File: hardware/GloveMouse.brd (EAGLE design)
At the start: 45.4 x 54.5 mm, 46 parts, among them IC3 MCP73811/2, J1 USB MICRO, U1 ATMEGA32U4-XUAU, U4 MCP1825S-3302E/DB

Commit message: GloveMouse v2.1 all-in-one commit
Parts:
- removed PARANI: (no value), pinhead:2X06
- added R1: 220, resistor:R0603
- added STATUSLED: BLUE, led:CHIP-LED0805
- added U$1: RN42, Tudor's_spankin'_library:RN42
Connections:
- new net N$7: STATUSLED.A, U$1.19
- new net N$8: R1.2, STATUSLED.C
- net +3V3: now also U$1.11; no longer PARANI.11
- net ADC10: now also LEFT_CLICK.2, R3.1; no longer R5.1, STAND-BY.2
- net ADC8: now also R5.1, STAND-BY.2; no longer LEFT_CLICK.2, R3.1
- net GND: now also R1.1, U$1.1, U$1.12, U$1.28, U$1.29; no longer PARANI.1, PARANI.12, PARANI.9
- net RXD: now also U$1.14; no longer PARANI.3
- net TXD: now also U$1.13; no longer PARANI.5
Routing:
- net +3V3: track 247.9 -> 204.3 mm, vias 1 -> 2
- net ADC8: track 49.5 -> 81.3 mm
- net ADC10: track 88.5 -> 61.8 mm
- net N$7: track 0.00 -> 9.44 mm, vias 0 -> 1
- net TXD: track 15.6 -> 23.6 mm, vias 0 -> 1
- net N$5: track 63.6 -> 66.9 mm
- net ADC9: track 71.9 -> 74.9 mm
- net N$8: track 0.00 -> 2.08 mm
- net RXD: track 14.8 -> 13.2 mm, vias 0 -> 1
- net PB4: track 25.6 -> 24.7 mm
- net PD0: track 49.2 -> 50.0 mm
- net GND: track 359.4 -> 360.0 mm
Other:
- board size 45.4 x 54.5 mm -> 44.4 x 52 mm

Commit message: GloveMouse v2.2 all-in-one commit
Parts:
- removed JP3: AVR-JTAG-10, avr-7:AVR-JTAG-10
- removed LED3, LED6: GREEN, led:CHIP-LED0805
- removed R22, R24: 1k, resistor:R0603
- added JP1: AVR-ISP-6, avr-5:AVR-ISP-6
- GYRO: device pinhead:1X07 -> pinhead:1X05
- moved GYRO 28.1 mm to (2.00, 30.0), turned to 90 degrees
- moved R21 24.8 mm to (7.00, 25.7)
- moved R23 23.0 mm to (6.79, 30.4), turned to 180 degrees
- moved LED4 20.6 mm to (7.34, 28.4)
- moved LED5 18.9 mm to (10.8, 30.4), turned to 90 degrees
- moved STAND-BY 17.0 mm to (31.7, 6.29)
- moved R5 16.1 mm to (30.8, 9.63), flipped to the top, turned to 180 degrees
- moved R3 14.2 mm to (18.8, 9.63), flipped to the top, turned to 180 degrees
- moved LEFT_CLICK 14.1 mm to (18.7, 6.26)
- moved R9 9.55 mm to (13.5, 17.9)
- moved R8 9.39 mm to (11.3, 17.9)
- moved J1 7.07 mm to (10.2, 4.49)
- moved C11 5.88 mm to (7.95, 21.6), turned to 270 degrees
- moved R4 4.74 mm to (25.3, 9.63), flipped to the top, turned to 180 degrees
- moved RIGHT_CLICK 4.27 mm to (25.1, 6.28)
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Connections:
- removed net N$4: LED3.A, R22.1
- removed net N$6: LED6.A, R24.1
- removed net PB0: LED6.C, U1.8
- removed net PB1: LED5.C, U1.9
- removed net PB2: LED3.C, U1.10
- removed net PB3: LED4.C, U1.11
- removed net PD0: GYRO.6, U1.18
- removed net PD1: GYRO.7, U1.19
- removed net TCK: JP3.1, U1.39
- removed net TDI: JP3.9, U1.36
- removed net TDO: JP3.3, U1.37
- removed net TMS: JP3.5, U1.38
- new net ADC6: GYRO.3, U1.37
- new net ADC7: GYRO.4, U1.36
- new net MISO: JP1.1, U1.11
- new net MOSI: JP1.4, U1.10
- new net PF0: LED4.A, U1.41
- new net PF1: LED5.A, U1.40
- new net SCK: JP1.3, U1.9
- net +3V3: now also JP1.2; no longer GYRO.2, JP3.4, JP3.7, R21.2, R22.2, R23.2, R24.2
- net GND: now also GYRO.2, JP1.6, R21.2, R23.2; no longer GYRO.3, JP3.10, JP3.2
- net N$1: now also LED5.C; no longer LED5.A
- net N$2: now also LED4.C; no longer LED4.A
- net RESET: now also JP1.5; no longer JP3.6
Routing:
- net PD1: track 55.1 -> 0.00 mm
- net PD0: track 50.0 -> 0.00 mm
- net RESET: track 73.7 -> 37.7 mm, vias 1 -> 0
- net ADC8: track 81.3 -> 47.1 mm
- net ADC9: track 74.9 -> 46.3 mm
- net +3V3: track 204.3 -> 186.9 mm
- net TDI: track 15.1 -> 0.00 mm
- net ADC10: track 61.8 -> 47.5 mm
- net ADC7: track 0.00 -> 13.6 mm
- net GND: track 360.0 -> 346.6 mm
- net ADC6: track 0.00 -> 13.4 mm
- net TMS: track 12.6 -> 0.00 mm, vias 1 -> 0
- net TCK: track 11.8 -> 0.00 mm
- net TDO: track 11.4 -> 0.00 mm
- net RD+: track 20.3 -> 9.08 mm
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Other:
- board size 44.4 x 52 mm -> 44.4 x 46.5 mm

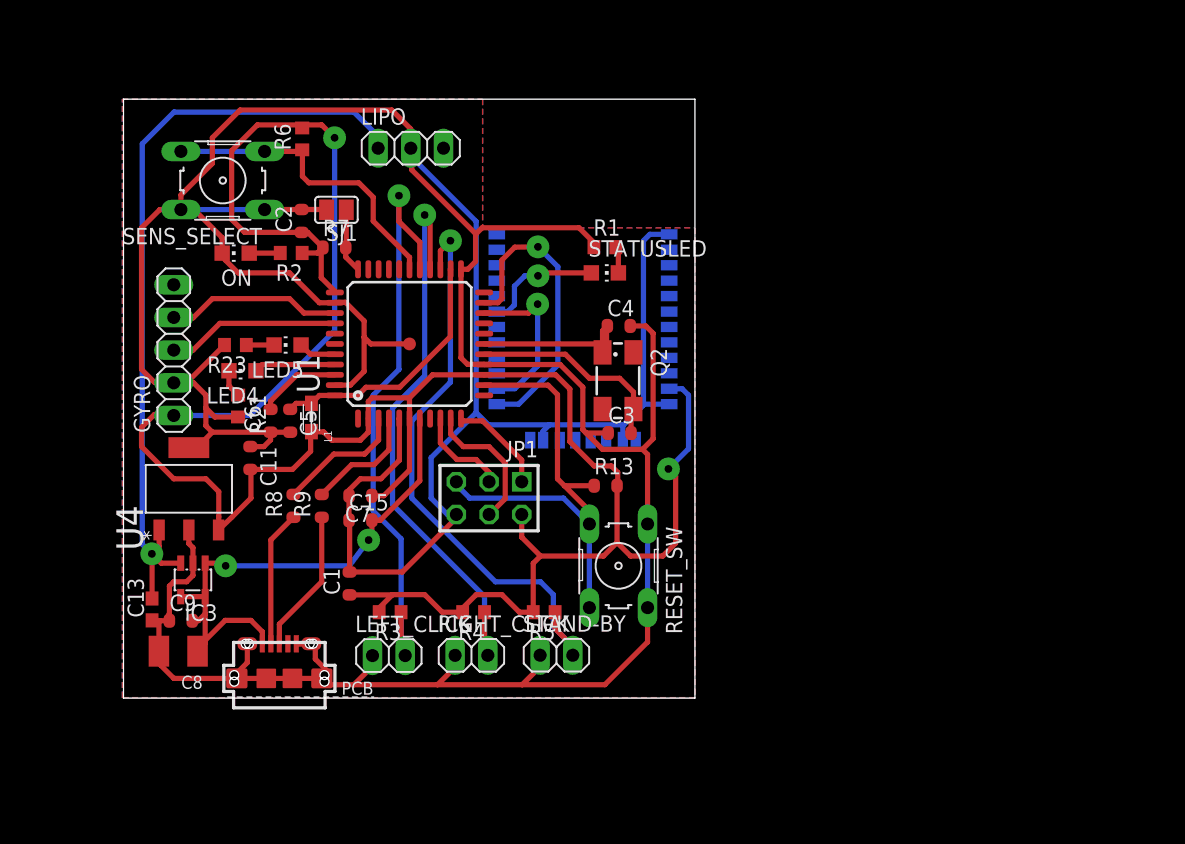
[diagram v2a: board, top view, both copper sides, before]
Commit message: v3.0: initial commit for GloveMouse v3.0
Changed ATmega32U4 with ATmega128RFA1.
Added onboard gyroscope from v2.4.
Added battery level measuring system.
Added controlable power led and low-battery led.
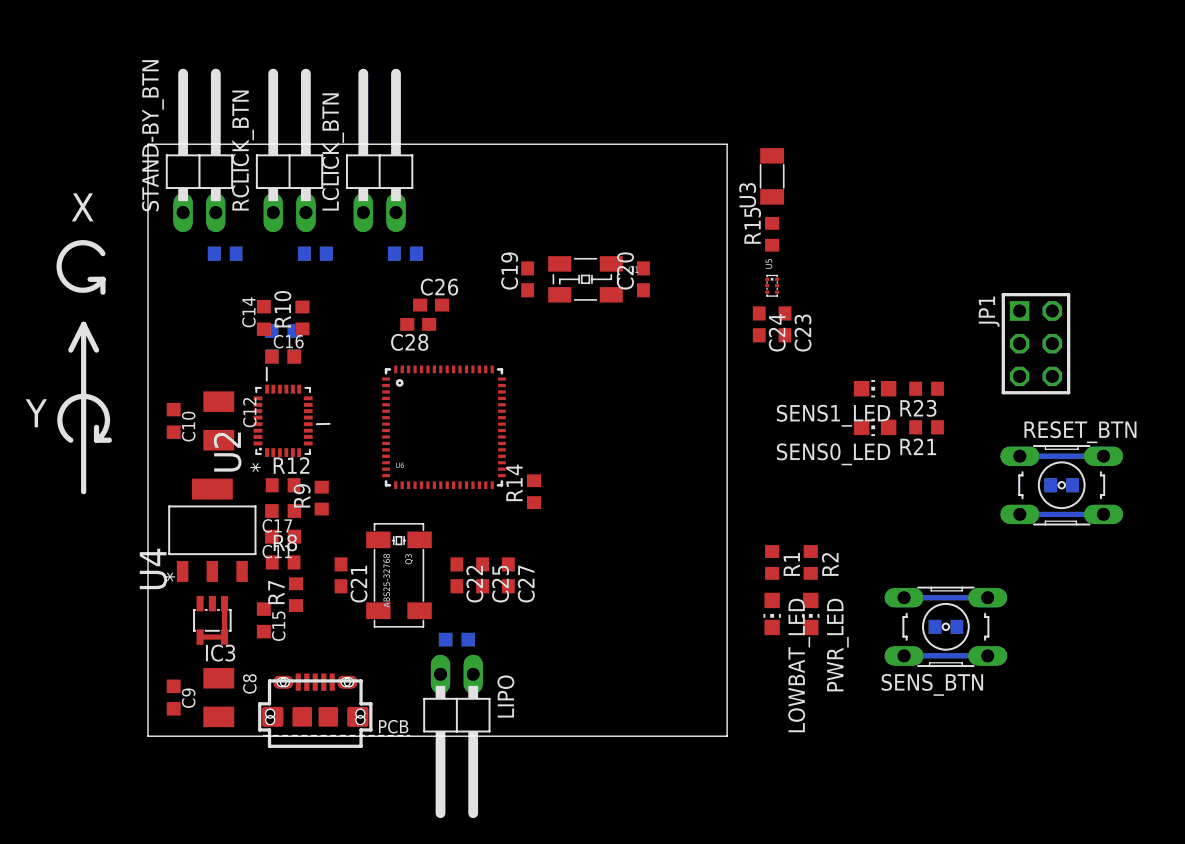
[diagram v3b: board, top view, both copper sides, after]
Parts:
- removed C1, C2, C6: 100n, SmartPrj:C0603-ROUND
- removed C3, C4: 22p, SmartPrj:C0603-ROUND
- removed C5, C7: 1uF, SmartPrj:C0603-ROUND
- removed GYRO: (no value), pinhead:1X05
- removed L1: MH2029-300Y, wuerth-elektronik:0805
- removed LED4: YELLOW, led:CHIP-LED0805
- removed LED5, ON: GREEN, led:CHIP-LED0805
- removed LEFT_CLICK, RIGHT_CLICK, STAND-BY: (no value), pinhead:1X02
- removed Q2: (no value), crystal:CTS406
- removed RESET_SW, SENS_SELECT: (no value), switch-omron:B3F-10XX
- removed SJ1: (no value), jumper:SJ
- removed STATUSLED: BLUE, led:CHIP-LED0805
- removed U$1: RN42, Tudor's_spankin'_library:RN42
- removed U1: ATMEGA32U4-XUAU, SmartPrj:TQFP44-PAD
- added C10: 100nF, resistor:C0603K
- added C12: 10uF, rcl:SMC_B
- added C14: 470nF, resistor:C0603K
- added C16: 10nF, resistor:C0603K
- added C17, C18: 0.1uF, resistor:C0603K
- added C19, C20, C23, C24: 22pF, resistor:C0603
- added C21, C22: 15pF, resistor:C0603
- added C25, C26, C27, C28: 100nF, resistor:C0603
- added LCLICK_BTN, RCLICK_BTN, STAND-BY_BTN: (no value), pinhead:1X02/90
- added LOWBAT_LED: RED, led:CHIP-LED0805
- added PWR_LED: GREEN, led:CHIP-LED0805
- added Q1: ABM3B-16, 0andrei_custom:ABM3B
- added Q3: ABS25-32768, danode:ABS25
- added R10: 10K, resistor:R0603
- added R11, R12: 33K, resistor:R0603
- added R14: 10k, resistor:R0603
- added R15: 0, resistor:R0603
- added RESET_BTN, SENS_BTN: (no value), switch-omron:B3F-10XX
- added SENS0_LED, SENS1_LED: YELLOW, led:CHIP-LED0805
- added U2: LPY403AL, Tudor's_spankin'_library:LGA28R50P8X6_500X400X100
- added U3: ANTENNA, 0andrei_custom:ANTPACK
- added U5: BALUN, 0andrei_custom:BALPACK
- added U6: ATMEGA128RFA1, SparkFun:QFN-64
- C11, C15: value 1u -> 1uF; device SmartPrj:C0603-ROUND -> resistor:C0603K
- C13: value 10u -> 10uF; device rcl:C0603 -> resistor:C0603K
- C8: value 10u -> 10uF
- C9: value 100n -> 100nF; device SmartPrj:C0603-ROUND -> resistor:C0603K
- LIPO: device pinhead:1X03 -> pinhead:1X02/90
- R1: value 220 -> 100R
- R13: device SmartPrj:R0603-ROUND -> resistor:R0603
- R2, R21, R23: value 1k -> 100R
- R3, R4, R5, R6: value 100k -> 10k
- R7: value 10K -> 100k; device SmartPrj:R0603-ROUND -> resistor:R0603
- R8: value 22R -> 100k; device SmartPrj:R0603-ROUND -> resistor:R0603
- R9: value 22R -> 10k; device SmartPrj:R0603-ROUND -> resistor:R0603
- moved R6 62.8 mm to (62.0, 8.50), flipped to the bottom, turned to 0 degrees
- moved R23 53.8 mm to (60.5, 27.0)
- moved R21 53.5 mm to (60.5, 24.0), turned to 180 degrees
- moved R2 47.0 mm to (51.5, 13.5), turned to 270 degrees
- moved LIPO 44.8 mm to (24.0, 1.00), turned to 180 degrees
- moved JP1 44.2 mm to (69.0, 30.5), turned to 270 degrees
- moved R5 37.3 mm to (6.00, 37.5), flipped to the bottom, turned to 0 degrees
- moved R13 35.4 mm to (71.0, 19.5), flipped to the bottom, turned to 180 degrees
- moved R4 30.5 mm to (13.0, 37.5), flipped to the bottom, turned to 0 degrees
- moved R3 27.9 mm to (20.0, 37.5), flipped to the bottom, turned to 0 degrees
- moved R1 27.7 mm to (48.5, 13.5), turned to 270 degrees
- moved R7 27.1 mm to (11.5, 11.0), turned to 90 degrees
- moved C13 23.8 mm to (24.0, 7.50), flipped to the bottom, turned to 0 degrees
- moved C15 10.8 mm to (9.00, 9.00), turned to 270 degrees
- moved C11 6.63 mm to (10.5, 15.5), turned to 180 degrees
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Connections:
- removed net ADC10: LEFT_CLICK.2, R3.1, U1.27
- removed net ADC6: GYRO.3, U1.37
- removed net ADC7: GYRO.4, U1.36
- removed net ADC8: R5.1, STAND-BY.2, U1.25
- removed net ADC9: R4.1, RIGHT_CLICK.2, U1.26
- removed net AREF: C6.2, U1.42
- removed net AVCC: C5.1, L1.2, U1.24, U1.44
- removed net D+: J1.P3, R9.1
- removed net D-: J1.P2, R8.1
- removed net HWB: R7.2, SJ1.1, U1.33
- removed net PB4: R6.1, SENS_SELECT.3, SENS_SELECT.4, U1.28
- removed net PF0: LED4.A, U1.41
- removed net PF1: LED5.A, U1.40
- removed net RD+: R9.2, U1.4
- removed net RD-: R8.2, U1.3
- removed net RXD: U$1.14, U1.20
- removed net TXD: U$1.13, U1.21
- removed net VUSB: C15.2, C8.+, C9.2, IC3.1, IC3.4, IC3.5, J1.P1, U1.7
- removed net XTAL1: C4.1, Q2.1, U1.17
- removed net XTAL2: C3.2, Q2.3, U1.16
- new net BAT: R7.2, R8.2, U6.6
- new net F1: C14.1, C16.1, U2.18
- new net F2: C16.2, R10.1, U2.17
- new net LCLICK: LCLICK_BTN.2, R3.2, U6.1
- new net LOWBAT: R1.1, U6.19
- new net N$10: C18.1, R11.2, U2.16
- new net N$11: C21.1, Q3.P$1, U6.17
- new net N$12: C22.1, Q3.P$4, U6.18
- new net N$13: C24.2, U6.8
- new net N$14: C23.2, U6.9
- new net N$15: C23.1, U5.P$4
- new net N$16: C24.1, U5.P$6
- new net N$17: C25.1, U6.21, U6.22
- new net N$18: C26.1, U6.60
- new net N$19: R9.2, U6.11
- new net N$20: R15.1, U5.P$1
- new net N$21: R14.2, U6.33
- new net N$22: R15.2, U3.P$1
- new net N$4: C14.2, R10.2
- new net N$6: R12.1, U2.1
- new net N$9: C19.1, Q1.1, U6.57
- new net PWR: R2.1, U6.43
- new net RCLICK: R4.2, RCLICK_BTN.2, U6.2
- new net SENS: R6.1, SENS_BTN.3, SENS_BTN.4
- new net SENS0: R21.1
- new net SENS1: R23.1
- new net STAND-BY: R5.2, STAND-BY_BTN.2, U6.3
- new net VBAT: C13.1, IC3.3, LIPO.1, R7.1, U4.1
- new net VBUS: C15.1, C8.+, C9.1, IC3.1, IC3.4, IC3.5, J1.P1
- new net XGYRO: U2.14, U6.4
- new net XOUT-1X2: C17.1, R12.2, U2.5
- new net ZGYRO: U2.7, U6.5
- net +3V3: now also C10.1, C11.1, C12.+, C27.1, C28.1, R3.1, R4.1, R5.1, U2.19, U2.9, U6.23, U6.34, U6.44, U6.54, U6.59, U6.62; no longer C1.1, C11.2, C2.1, C7.1, GYRO.1, L1.1, R2.1, R3.2, R4.2, R5.2, R7.1, U$1.11, U1.14, U1.2, U1.34, U1.6
- net GND: now also C10.2, C11.2, C12.-, C13.2, C15.2, C17.2, C18.2, C19.2, C20.2, C21.2, C22.2, C25.2, C26.2, C27.2, C28.2, C9.2, LCLICK_BTN.1, LOWBAT_LED.C, PWR_LED.C, Q1.2, Q1.4, Q3.P$2, Q3.P$3, R14.1, R8.1, R9.1, RCLICK_BTN.1, RESET_BTN.1, RESET_BTN.2, SENS0_LED.C, SENS1_LED.C, SENS_BTN.1, SENS_BTN.2, STAND-BY_BTN.1, U2.24, U2.26, U2.27, U2.28, U5.P$3, U6.10, U6.20, U6.24, U6.35, U6.45, U6.55, U6.58, U6.61, U6.7; no longer C1.2, C11.1, C13.1, C15.1, C2.2, C3.1, C4.2, C5.2, C6.1, C7.2, C9.1, GYRO.2, LEFT_CLICK.1, ON.C, R1.1, R21.2, R23.2, RESET_SW.1, RESET_SW.2, RIGHT_CLICK.1, SENS_SELECT.1, SENS_SELECT.2, SJ1.2, STAND-BY.1, U$1.1, U$1.12, U$1.28, U$1.29, U1.15, U1.23, U1.35, U1.43, U1.5, U1.P$1
- net MISO: now also U6.39; no longer U1.11
- net MOSI: now also U6.38; no longer U1.10
- net N$1: now also R23.2, SENS1_LED.A; no longer LED5.C, R23.1
- net N$2: now also LOWBAT_LED.A, R1.2; no longer LED4.C, R21.1
- net N$3: now also PWR_LED.A; no longer ON.A
- net N$5: now also R21.2, SENS0_LED.A; no longer C13.2, IC3.3, LIPO.1, U4.1
- net N$7: now also R11.1, U2.20; no longer STATUSLED.A, U$1.19
- net N$8: now also C20.1, Q1.3, U6.56; no longer R1.2, STATUSLED.C
- net RESET: now also RESET_BTN.3, RESET_BTN.4, U6.12; no longer RESET_SW.3, RESET_SW.4, U1.13
- net SCK: now also U6.37; no longer U1.9
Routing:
- net GND: track 346.6 -> 13.0 mm
- net +3V3: track 186.9 -> 0.00 mm, vias 2 -> 0
- net N$5: track 61.4 -> 0.00 mm, vias 1 -> 0
- net ADC10: track 47.5 -> 0.00 mm, vias 1 -> 0
- net ADC8: track 47.1 -> 0.00 mm, vias 1 -> 0
- net ADC9: track 46.3 -> 0.00 mm, vias 1 -> 0
- net VUSB: track 42.9 -> 0.00 mm, vias 2 -> 0
- net RESET: track 37.7 -> 6.50 mm
- net PB4: track 24.7 -> 0.00 mm
- net TXD: track 23.6 -> 0.00 mm, vias 1 -> 0
- net AVCC: track 20.0 -> 0.00 mm
- net XTAL2: track 16.7 -> 0.00 mm
- net XTAL1: track 15.4 -> 0.00 mm
- net ADC7: track 13.6 -> 0.00 mm
- net ADC6: track 13.4 -> 0.00 mm
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- removed copper zone on layer 1, net GND
- removed copper zone on layer 16, net GND
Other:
- board size 44.4 x 46.5 mm -> 45 x 46 mm
- board text added: "X"
- board text added: "Y"

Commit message: v3.0 release candidate 1
Changed secondary crystal.
Finished routing.
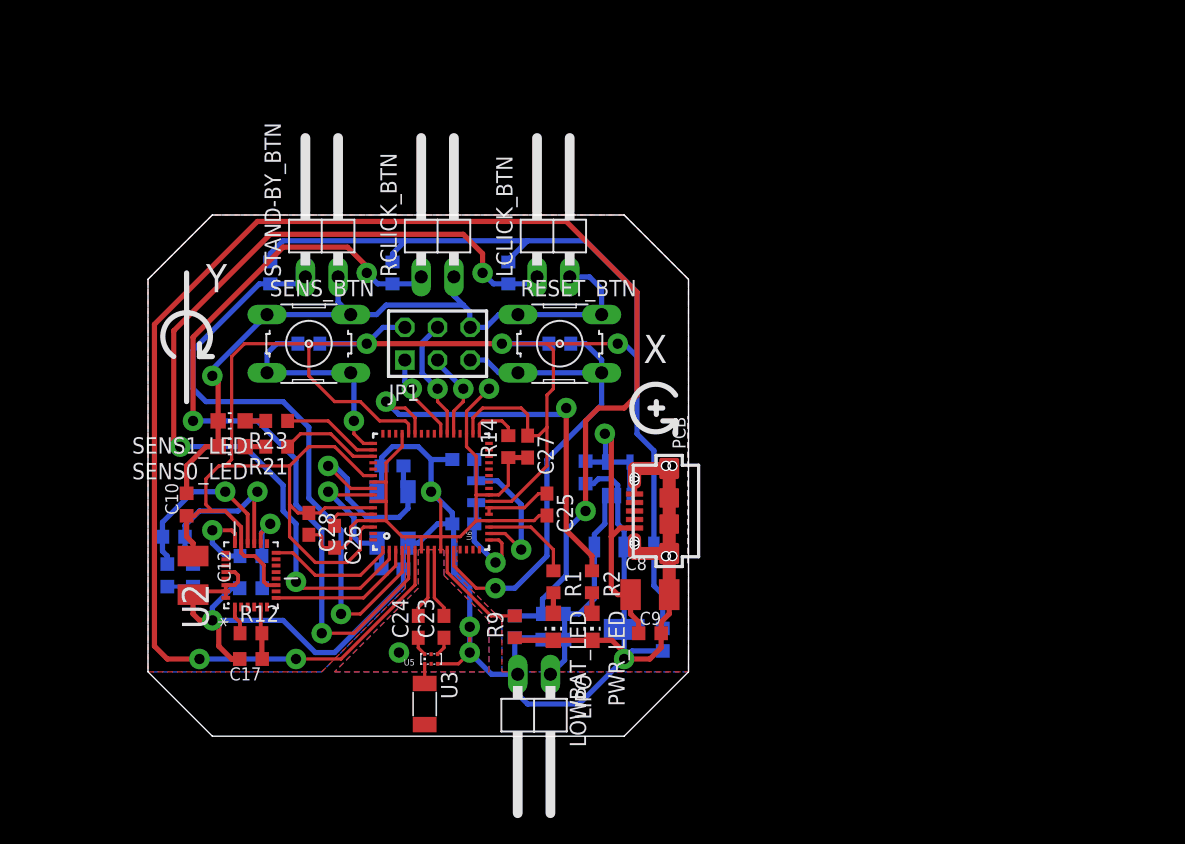
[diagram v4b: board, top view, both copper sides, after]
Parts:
- removed Q3: ABS25-32768, danode:ABS25
- removed R15: 0, resistor:R0603
- added Q2: 32.768kHz, crystal:FC-12M
- moved R6 54.2 mm to (12.5, 30.5), turned to 180 degrees
- moved SENS_BTN 54.2 mm to (12.5, 30.5), turned to 0 degrees
- moved R23 50.6 mm to (10.0, 24.5)
- moved R21 50.5 mm to (10.0, 22.5)
- moved SENS1_LED 50.1 mm to (6.50, 24.5)
- moved SENS0_LED 50.0 mm to (6.50, 22.5)
- moved U3 49.1 mm to (21.5, 2.50), turned to 270 degrees
- moved JP1 46.5 mm to (22.5, 30.5), turned to 0 degrees
- moved R13 40.5 mm to (32.0, 30.5), turned to 0 degrees
- moved RESET_BTN 40.5 mm to (32.0, 30.5)
- moved U5 39.3 mm to (22.0, 6.00), turned to 180 degrees
- moved C9 37.3 mm to (39.0, 8.00), turned to 0 degrees
- moved C23 35.4 mm to (23.0, 8.50), turned to 90 degrees
- moved C24 35.4 mm to (21.0, 8.50), turned to 90 degrees
- moved C8 34.4 mm to (39.0, 11.0), turned to 0 degrees
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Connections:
- removed net N$20: R15.1, U5.P$1
- net GND: now also LCLICK_BTN.2, RCLICK_BTN.2, STAND-BY_BTN.2; no longer LCLICK_BTN.1, Q3.P$2, Q3.P$3, RCLICK_BTN.1, STAND-BY_BTN.1
- net LCLICK: now also LCLICK_BTN.1, U6.2; no longer LCLICK_BTN.2, U6.1
- net N$11: now also Q2.2; no longer Q3.P$1
- net N$12: now also Q2.1; no longer Q3.P$4
- net N$22: now also U5.P$1; no longer R15.2
- net RCLICK: now also RCLICK_BTN.1, U6.5; no longer RCLICK_BTN.2, U6.2
- net SENS: now also U6.49
- net SENS0: now also U6.51
- net SENS1: now also U6.50
- net STAND-BY: now also STAND-BY_BTN.1, U6.4; no longer STAND-BY_BTN.2, U6.3
- net XGYRO: now also U6.1; no longer U6.4
- net ZGYRO: now also U6.3; no longer U6.5
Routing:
- net GND: track 13.0 -> 260.4 mm, vias 0 -> 8
- net +3V3: track 0.00 -> 206.2 mm, vias 0 -> 3
- net BAT: track 0.00 -> 125.4 mm, vias 0 -> 3
- net LCLICK: track 0.00 -> 69.5 mm, vias 0 -> 3
- net RCLICK: track 0.00 -> 63.2 mm, vias 0 -> 3
- net STAND-BY: track 0.00 -> 47.7 mm, vias 0 -> 1
- net RESET: track 6.50 -> 40.8 mm, vias 0 -> 1
- net PWR: track 0.00 -> 32.1 mm, vias 0 -> 2
- net VBUS: track 4.50 -> 27.6 mm, vias 0 -> 1
- net N$8: track 0.00 -> 16.7 mm, vias 0 -> 1
- net VBAT: track 0.00 -> 16.4 mm
- net F2: track 0.00 -> 14.1 mm, vias 0 -> 1
- net F1: track 0.00 -> 14.0 mm, vias 0 -> 1
- net N$12: track 0.00 -> 12.5 mm, vias 0 -> 1
- net N$9: track 0.00 -> 12.3 mm, vias 0 -> 1
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- added copper zone on layer 1, net GND
- added copper zone on layer 16, net GND
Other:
- board size 45 x 46 mm -> 42 x 40.5 mm
